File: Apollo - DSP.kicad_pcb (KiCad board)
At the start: 4 copper layers, 74.9 x 58 mm, 69 parts, among them J1 USB_C_Receptacle_USB2.0, J2 Conn_01x04, J3 MEM2067-02-180-00-A_REVB, J5 Conn_01x04, J6 Conn_01x04, U1 NCP115ASN330T2G, U2 USBLC6-2SC6, U3 NCP115ASN330T2G, U4 STM32F401RBTx, U6 MCP602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

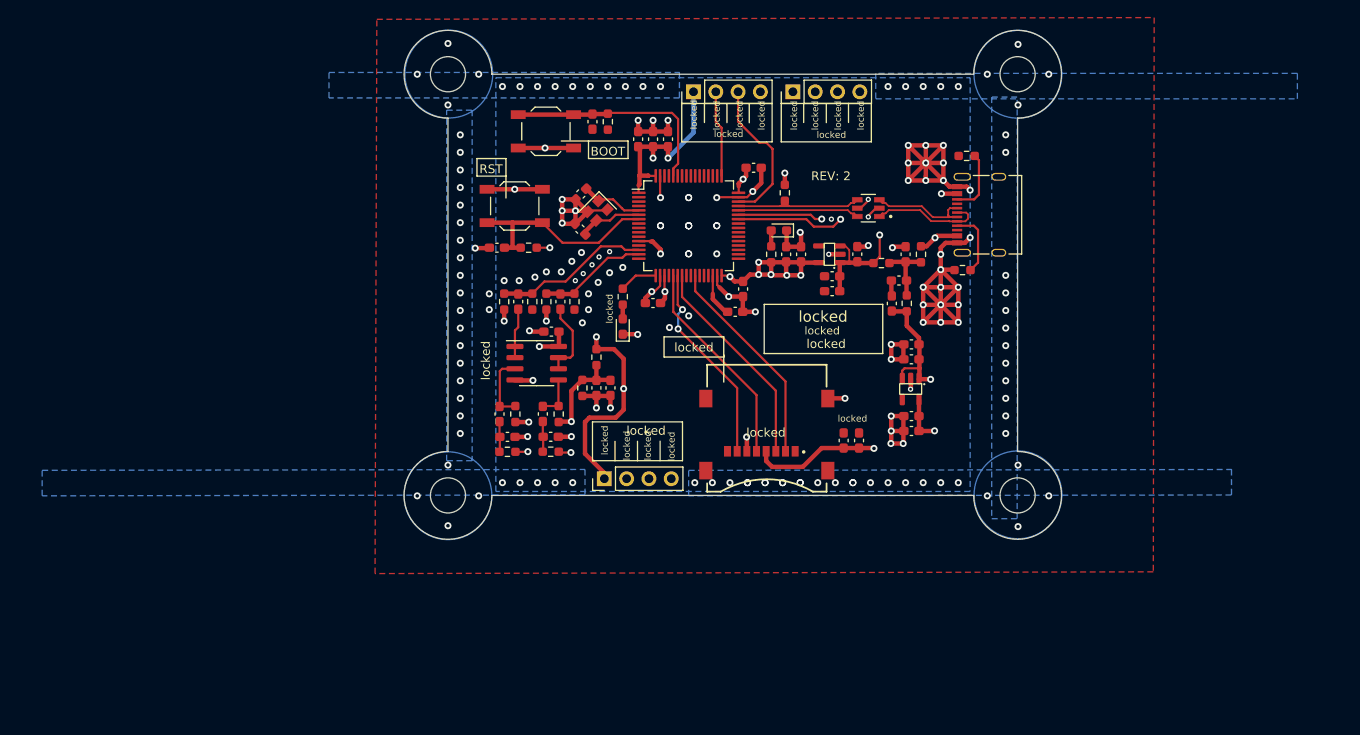
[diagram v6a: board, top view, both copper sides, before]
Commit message: added sram chip again, might come in handy for mor complex calculations
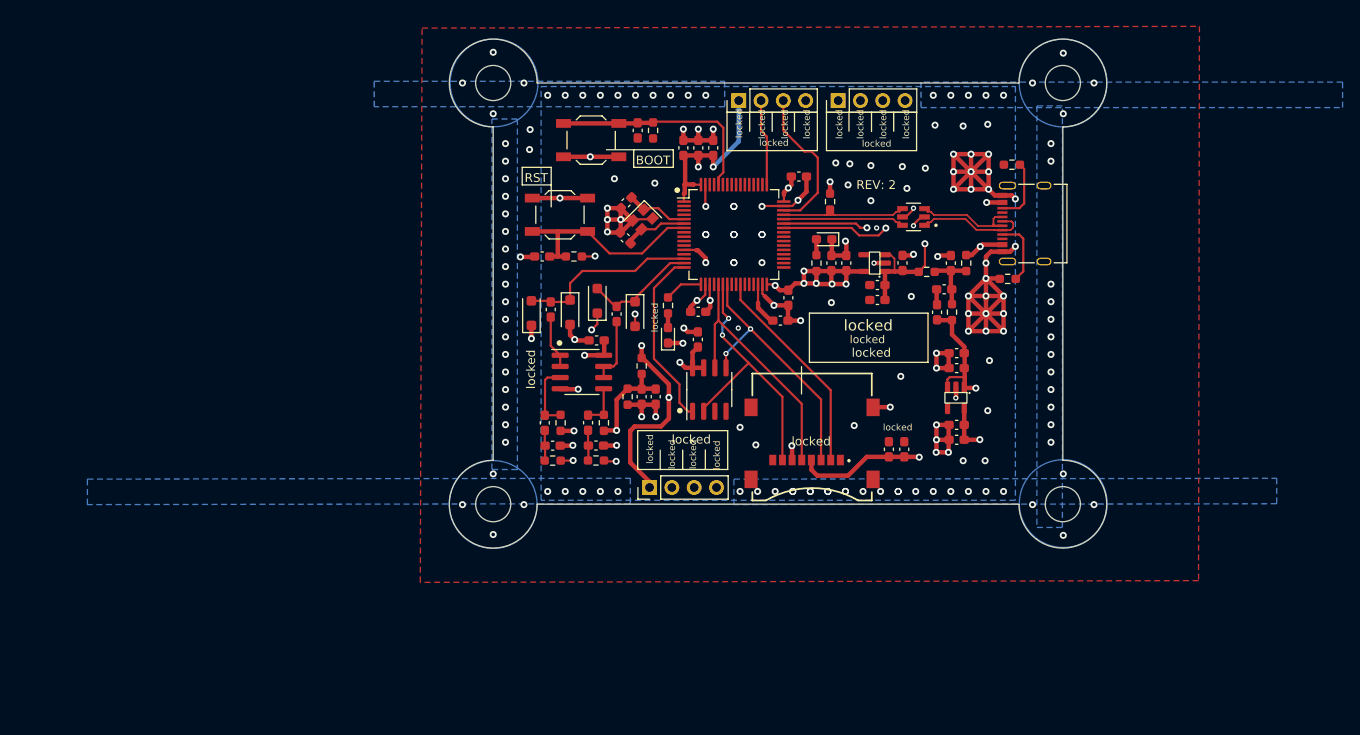
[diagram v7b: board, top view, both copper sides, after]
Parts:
- added C25: 100n, Capacitor_SMD:C_0603_1608Metric_Pad1.08x0.95mm_HandSolder, F.Cu at (123.2, 90.9)
- added U5: 23K256, Package_SO:SOIC-8_3.9x4.9mm_P1.27mm, F.Cu at (124.5, 96.6)
- D3, D4, D5, D6: value 3V6 -> 3V4; footprint Resistor_SMD:R_0603_1608Metric_Pad0.98x0.95mm_HandSolder -> Diode_SMD:D_SOD-123F
- moved D6 11.8 mm to (116.0, 88.0)
- moved C32 6.55 mm to (113.9, 88.0)
- moved BOOT1 5.25 mm to (111.0, 68.2)
- moved C10 5.25 mm to (152.6, 94.2)
- moved C11 5.25 mm to (152.6, 92.5)
- moved C12 5.25 mm to (152.6, 100.6)
- moved C13 5.25 mm to (152.6, 102.3)
- moved C15 5.25 mm to (123.2, 87.8)
- moved C16 5.25 mm to (134.7, 72.3)
- moved C17 5.25 mm to (121.5, 69.1)
- moved C18 5.25 mm to (124.9, 69.1)
- moved C19 5.25 mm to (123.2, 69.1)
- moved C21 5.25 mm to (114.9, 79.3)
- moved C22 5.25 mm to (144.9, 103.4)
- moved C24 5.25 mm to (111.6, 91.0)
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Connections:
- D3 pad 1: +3.3VA -> ADC_CH0_IN
- D3 pad 2: ADC_CH1_IN -> GND
- D5 pad 1: ADC_CH1_IN -> +3.3VA
- D5 pad 2: GND -> ADC_CH1_IN
- D6 pad 1: ADC_CH0_IN -> ADC_CH1_IN
- U4 pad 16: unconnected-(U4-PA2-Pad16) -> RAM_nCS
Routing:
- net RAM_nCS: track 0.00 -> 20.6 mm
- net MISO: track 23.2 -> 31.0 mm
- net 3.3V: track 74.6 -> 80.2 mm, vias 14 -> 15
- net MOSI: track 24.4 -> 30.0 mm, vias 0 -> 2
- net SCK: track 23.9 -> 29.5 mm
- net GND: track 198.7 -> 203.8 mm, vias 182 -> 188
- net +3.3VA: track 79.8 -> 83.2 mm
- net ADC_CH0_IN: track 17.8 -> 20.6 mm
- net /Analog/CH1_OP_OUT: track 8.83 -> 7.63 mm

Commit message: updated pics
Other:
- board text added: "CS(PA2)"
- board text removed: "REV: 2"
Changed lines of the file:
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@@
   (gr_line (start 134.14964 65.043951) (end 134.14964 67.228951)
-    (stroke (width 0.15) (type default)) (layer "F.SilkS"))
-  (gr_line (start 134.95 97.1) (end 134.95 94)
     (stroke (width 0.15) (type default)) (layer "F.SilkS"))
   (gr_rect (start 115.85 69.3) (end 120.35 71.3)
@@
   (gr_circle (center 164.7 109.65) (end 164.7 107.65)
     (stroke (width 0.1) (type default)) (fill none) (layer "Edge.Cuts"))
-  (gr_text "REV: 2" (at 143.45 73.3) (layer "F.SilkS")
-    (effects (font (size 1 1) (thickness 0.25)))
-  )
   (gr_text "BOOT" (at 118.05 70.5) (layer "F.SilkS")
     (effects (font (size 1 1) (thickness 0.25)))
@@
     (effects (font (size 1 1) (thickness 0.15)))
   )
+  (gr_text "CS(PA2)" (at 128.1 94.6 90) (layer "F.SilkS")
+    (effects (font (size 0.75 0.75) (thickness 0.1875)))
+  )
   (gr_text locked "G" (at 125.3 104.08 90) (layer "F.SilkS")
     (effects (font (size 0.75 0.75) (thickness 0.1875)))
@@
   (gr_text locked "G" (at 135.55 66.4 90) (layer "F.SilkS")
     (effects (font (size 0.75 0.75) (thickness 0.1875)))
-  )
-  (gr_text locked "ANALOG" (at 104.15 94.3 90) (layer "F.SilkS")
-    (effects (font (size 1 1) (thickness 0.25)))
   )
   (gr_text locked "CS(PB0)" (at 145.9 100.9) (layer "F.SilkS")
@@
   (segment (start 138.2 76.1125) (end 138.2 76.474999) (width 0.2) (layer "F.Cu") (net 29))
   (segment (start 138.2 76.724999) (end 138.2 76.1125) (width 0.2) (layer "F.Cu") (net 29))
+  (segment (start 126.05 71.45) (end 126.05 66.8) (width 0.254) (layer "F.Cu") (net 33))
   (segment (start 118 66.2375) (end 118.05 66.1875) (width 0.508) (layer "F.Cu") (net 33))
   (segment (start 116.2375 66.3) (end 116.3 66.2375) (width 0.508) (layer "F.Cu") (net 33))
-  (segment (start 125.5 72.431486) (end 126.05 71.881486) (width 0.254) (layer "F.Cu") (net 33))
   (segment (start 116.3 66.2375) (end 118 66.2375) (width 0.508) (layer "F.Cu") (net 33))
-  (segment (start 118.05 66.1875) (end 118.1375 66.1) (width 0.254) (layer "F.Cu") (net 33))
-  (segment (start 126.05 71.881486) (end 126.05 66.8) (width 0.254) (layer "F.Cu") (net 33))
+  (segment (start 118.1375 66.1) (end 118.05 66.1875) (width 0.254) (layer "F.Cu") (net 33))
+  (segment (start 125.35 66.1) (end 118.1375 66.1) (width 0.254) (layer "F.Cu") (net 33))
+  (segment (start 126.05 66.8) (end 125.35 66.1) (width 0.254) (layer "F.Cu") (net 33))
+  (segment (start 125.5 73.275) (end 125.5 72) (width 0.254) (layer "F.Cu") (net 33))
   (segment (start 107.85 66.3) (end 114.15 66.3) (width 0.508) (layer "F.Cu") (net 33))
-  (segment (start 126.05 66.8) (end 125.35 66.1) (width 0.254) (layer "F.Cu") (net 33))
   (segment (start 114.15 66.3) (end 116.2375 66.3) (width 0.508) (layer "F.Cu") (net 33))
-  (segment (start 125.5 73.275) (end 125.5 72.431486) (width 0.254) (layer "F.Cu") (net 33))
-  (segment (start 118.1375 66.1) (end 125.35 66.1) (width 0.254) (layer "F.Cu") (net 33))
+  (segment (start 125.5 72) (end 126.05 71.45) (width 0.254) (layer "F.Cu") (net 33))
   (segment (start 116 86.2) (end 120 82.2) (width 0.254) (layer "F.Cu") (net 37))
   (segment (start 113.7375 87.1375) (end 113.9 87.1375) (width 0.254) (layer "F.Cu") (net 37))
